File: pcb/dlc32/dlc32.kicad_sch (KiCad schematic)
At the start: 28 parts, among them IC1 74LV11, IC2 74HCT08, IC5 74HCT04, J1 DOOR1, J2 DOOR2, J3 CHILLER, J4 TO_J8, J6 Conn_02x04_Odd_Even, J7 LASER_AUX, J8 LASER

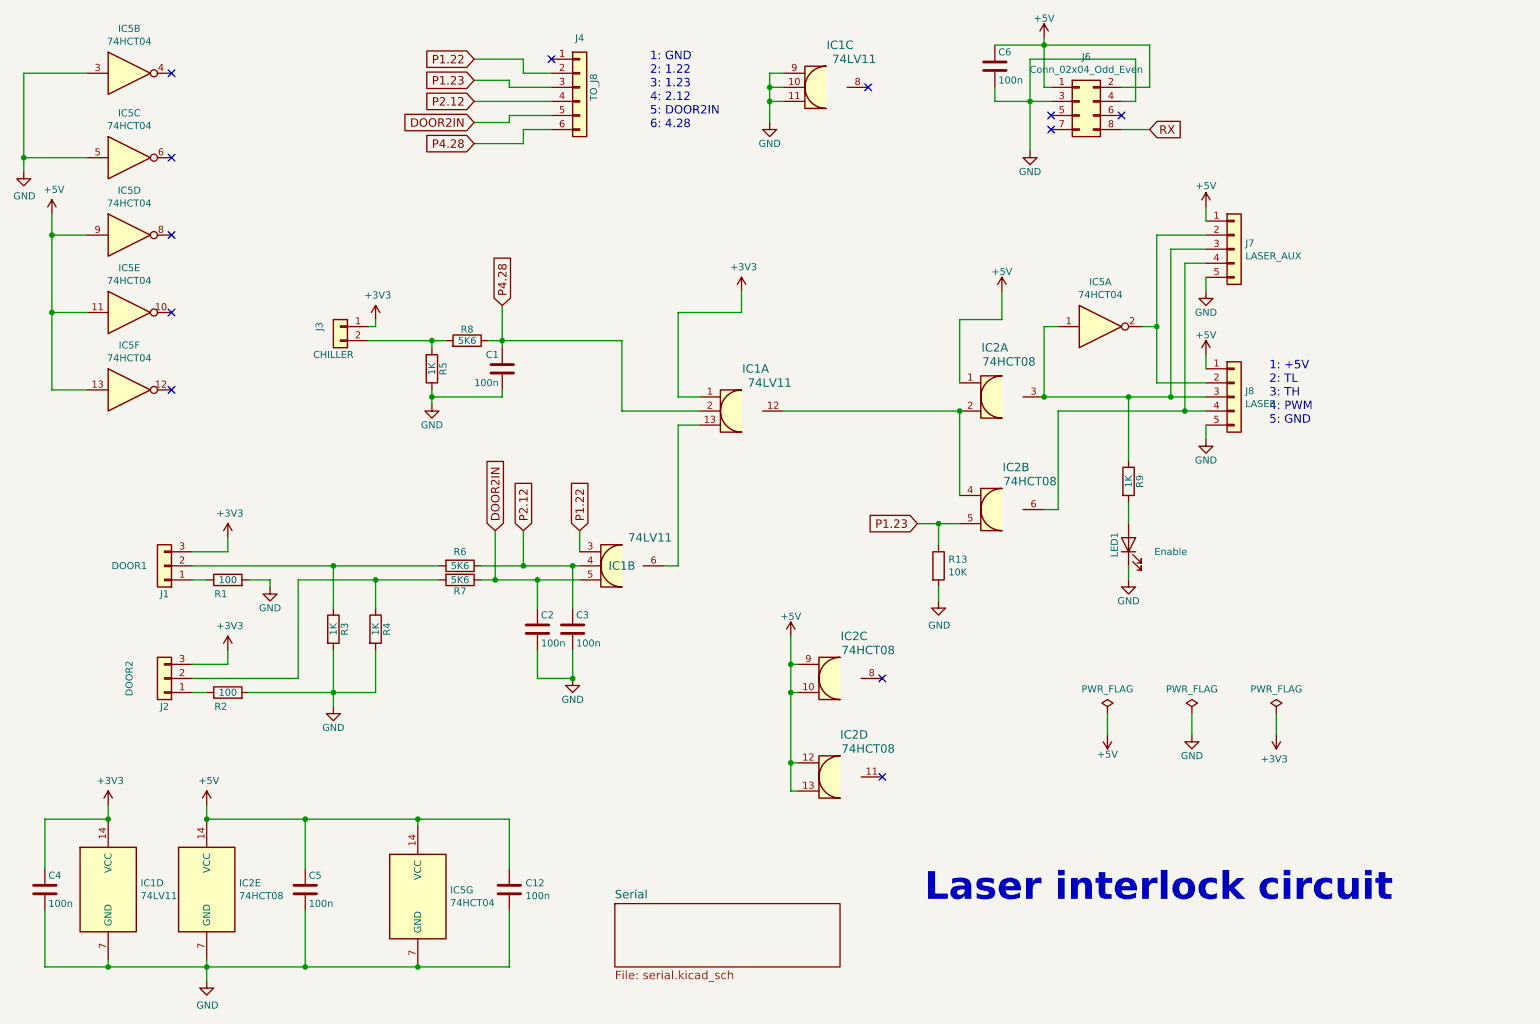
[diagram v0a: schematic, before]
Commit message: Update symbols etc, remove obsolete parts.
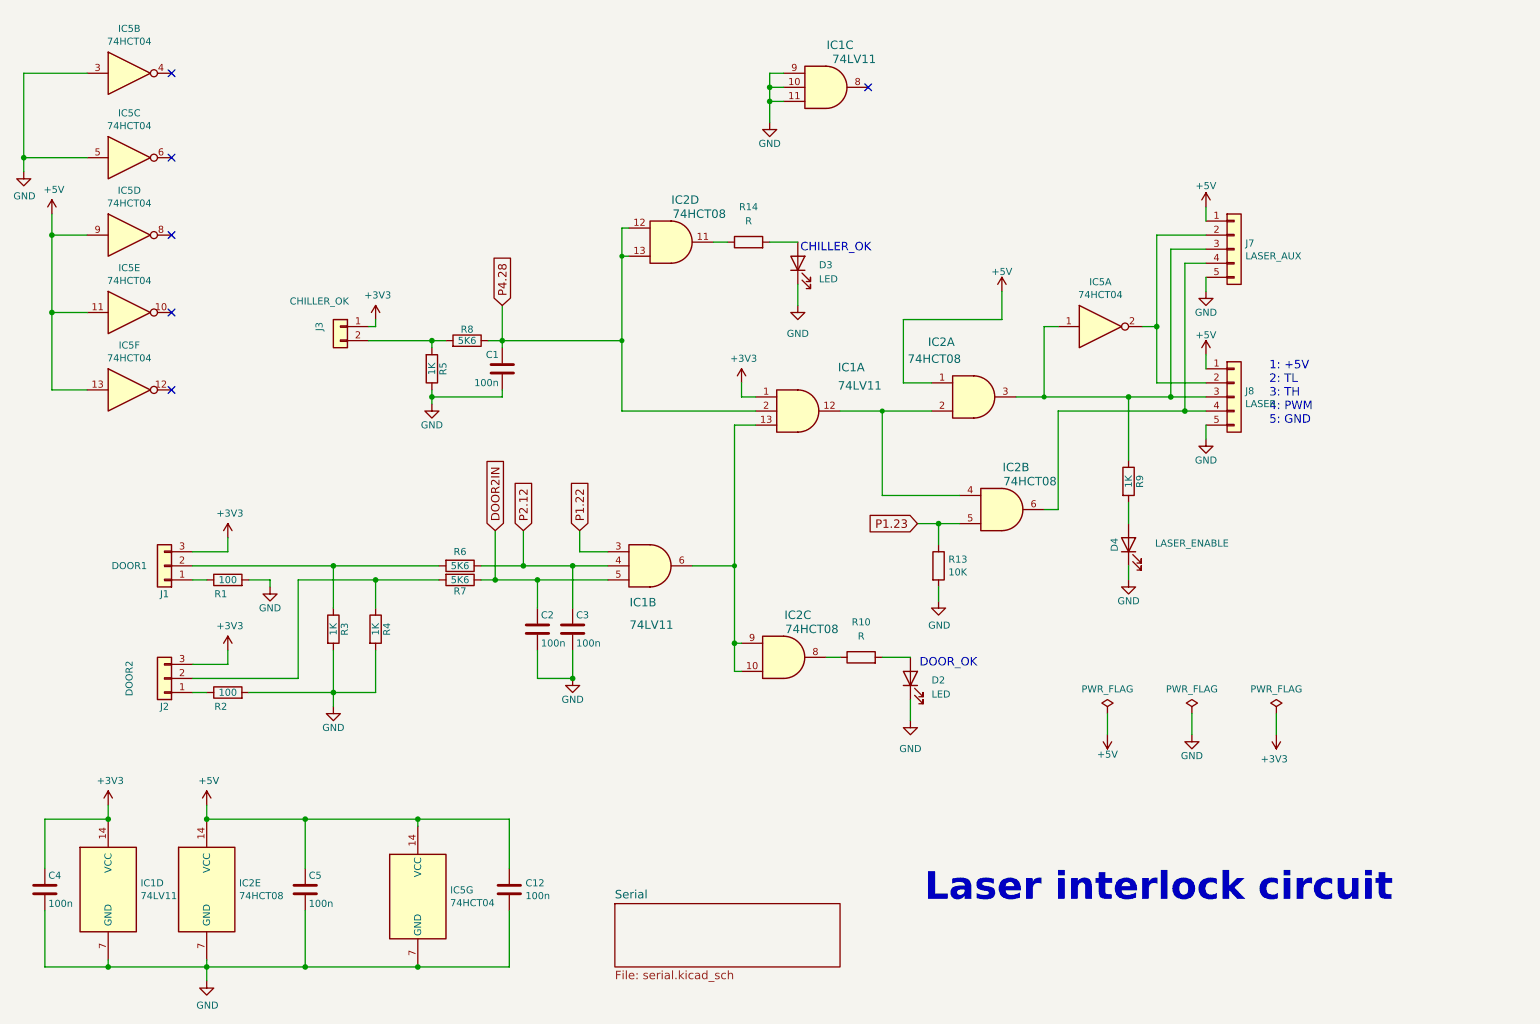
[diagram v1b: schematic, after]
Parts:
- removed C6: 100n, Capacitor_SMD:C_0603_1608Metric, symbol Device:C
- removed J4: TO_J8, Connector_JST:JST_XH_B06B-XH-A_1x06_P2.50mm_Vertical, symbol Connector_Generic:Conn_01x06
- removed J6: Conn_02x04_Odd_Even, Connector_PinSocket_2.54mm:PinSocket_2x04_P2.54mm_Vertical, symbol Connector_Generic:Conn_02x04_Odd_Even
- added D2, D3: LED, LED_THT:LED_D5.0mm_Horizontal_O1.27mm_Z3.0mm, symbol Device:LED
- added R10, R14: R, Resistor_SMD:R_0603_1608Metric, symbol Device:R
- D4: renamed from LED1; value Enable -> LASER_ENABLE; footprint LED_SMD:LED_0603_1608Metric -> LED_THT:LED_D5.0mm_Horizontal_O1.27mm_Z3.0mm
- J3: value CHILLER -> CHILLER_OK
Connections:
- net +5V: no longer IC2.10, IC2.12, IC2.13, IC2.9
- net GND: now also D2.1 (K), D3.1 (K)
- net P4.28: now also IC2.12, IC2.13
- net at IC1.13, IC1.6: now also IC2.10, IC2.9
- net at IC2.8: now also R10.1
- net at IC2.11: now also R14.1
- new net: D3.2 (A), R14.2
- new net: D2.2 (A), R10.2
- no-connect marks 12 -> 6
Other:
- note added: "CHILLER_OK"
- note added: "DOOR_OK"
- note removed: "1: GND 2: 1.22 3: 1.23 4: 2.12 5: DOOR2IN 6: 4.28"
- moved on the sheet: IC1A, IC1B, IC2A, IC2C

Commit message: Renumber, delete PCB.
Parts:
- renumbered C12 to C7, IC5 to IC3
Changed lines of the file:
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@@
 		(on_board yes)
 		(dnp no)
-		(property "Reference" "C12"
+		(property "Reference" "C7"
 			(at 108.331 172.8216 0)
 			(effects
@@
 			(project ""
 				(path "/fc0b2ef6-7d8e-4322-8468-8fac0c3c3d07"
-					(reference "C12")
+					(reference "C7")
 					(unit 1)
 				)
@@
 		(on_board yes)
 		(dnp no)
-		(property "Reference" "IC5"
+		(property "Reference" "IC3"
 			(at 36.83 18.6182 0)
 			(effects
@@
 			(project ""
 				(path "/fc0b2ef6-7d8e-4322-8468-8fac0c3c3d07"
-					(reference "IC5")
+					(reference "IC3")
 					(unit 2)
 				)
@@
 		(on_board yes)
 		(dnp no)
-		(property "Reference" "IC5"
+		(property "Reference" "IC3"
 			(at 36.83 33.8582 0)
 			(effects
@@
 			(project ""
 				(path "/fc0b2ef6-7d8e-4322-8468-8fac0c3c3d07"
-					(reference "IC5")
+					(reference "IC3")
 					(unit 3)
 				)
@@
 		(on_board yes)
 		(dnp no)
-		(property "Reference" "IC5"
+		(property "Reference" "IC3"
 			(at 36.83 47.8282 0)
 			(effects
@@
 			(project ""
 				(path "/fc0b2ef6-7d8e-4322-8468-8fac0c3c3d07"
-					(reference "IC5")
+					(reference "IC3")
 					(unit 4)
 				)
@@
 		(on_board yes)
 		(dnp no)
-		(property "Reference" "IC5"
+		(property "Reference" "IC3"
 			(at 36.83 61.7982 0)
 			(effects
@@
 			(project ""
 				(path "/fc0b2ef6-7d8e-4322-8468-8fac0c3c3d07"
-					(reference "IC5")
+					(reference "IC3")
 					(unit 5)
 				)
@@
 		(on_board yes)
 		(dnp no)
-		(property "Reference" "IC5"
+		(property "Reference" "IC3"
 			(at 36.83 75.7682 0)
 			(effects
@@
 			(project ""
 				(path "/fc0b2ef6-7d8e-4322-8468-8fac0c3c3d07"
-					(reference "IC5")
+					(reference "IC3")
 					(unit 6)
 				)

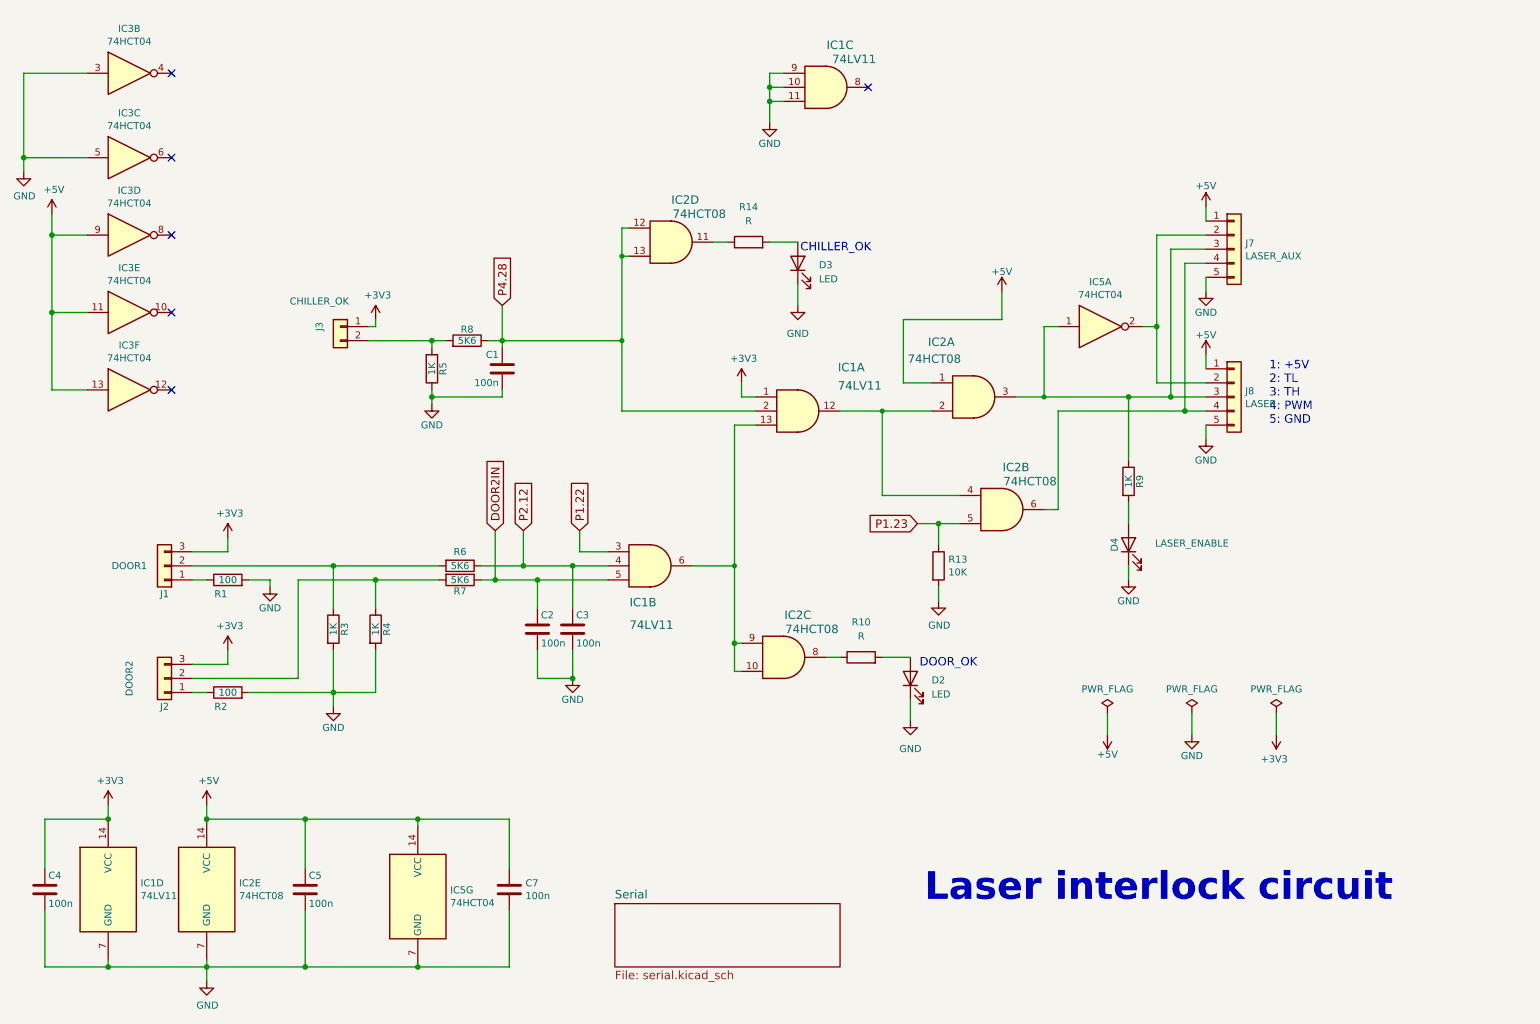
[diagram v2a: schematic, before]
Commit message: Include exhaust control in dlc32 pcb.
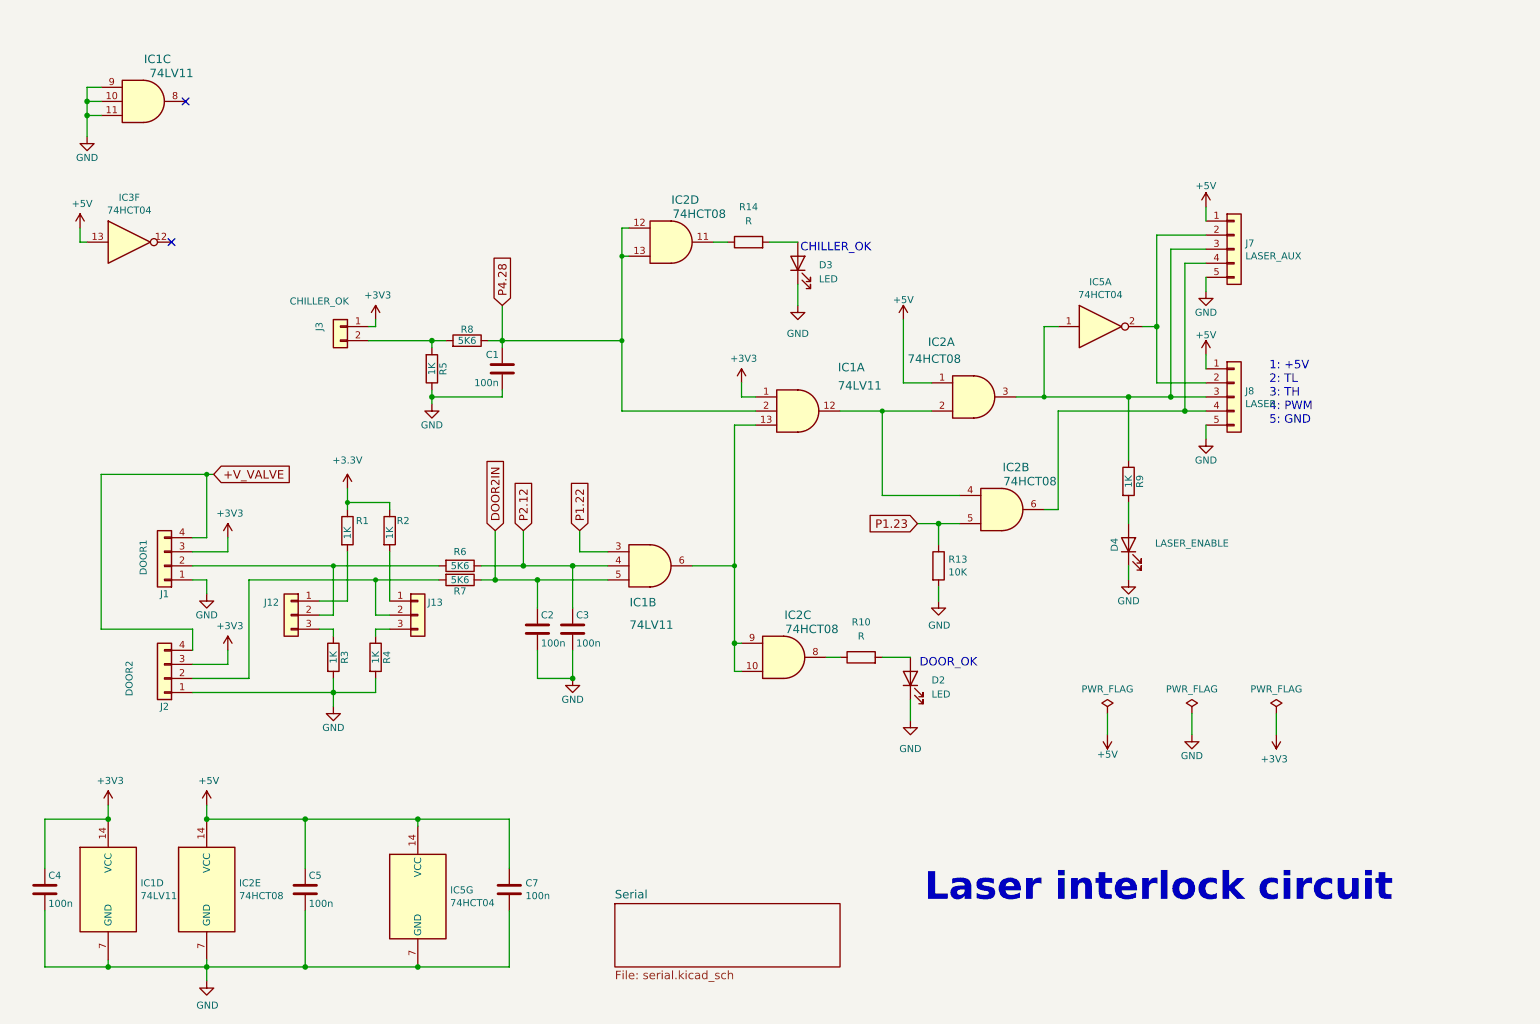
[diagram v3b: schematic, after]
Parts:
- removed unit 2 of IC3
- removed unit 3 of IC3
- removed unit 4 of IC3
- removed unit 5 of IC3
- added J12: Conn_01x03, Connector_PinHeader_2.54mm:PinHeader_1x03_P2.54mm_Vertical, symbol Connector_Generic:Conn_01x03
- added J13: Conn_01x03, Connector_JST:JST_XH_B3B-XH-A_1x03_P2.50mm_Vertical, symbol Connector_Generic:Conn_01x03
- J1, J2: footprint Connector_JST:JST_PH_B3B-PH-K_1x03_P2.00mm_Vertical -> Connector_JST:JST_XH_B4B-XH-A_1x04_P2.50mm_Vertical; symbol Connector_Generic:Conn_01x03 -> Connector_Generic:Conn_01x04
- J3: footprint Connector_JST:JST_PH_B2B-PH-K_1x02_P2.00mm_Vertical -> Connector_JST:JST_XH_B2B-XH-A_1x02_P2.50mm_Vertical
- J7, J8: footprint Connector_JST:JST_PH_B5B-PH-K_1x05_P2.00mm_Vertical -> Connector_JST:JST_XH_B5B-XH-A_1x05_P2.50mm_Vertical
- R1, R2: value 100 -> 1K
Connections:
- net GND: now also J1.1 (Pin_1), J2.1 (Pin_1); no longer R1.2, R2.2
- net at J1.2 (Pin_2), R6.2: now also J12.2 (Pin_2); no longer R3.1
- net at J2.2 (Pin_2), R7.2: now also J13.2 (Pin_2); no longer R4.1
- net +3.3V: now reaches R1.1
- net +3.3V: now also R2.1; no longer J1.1 (Pin_1)
- new net: J12.3 (Pin_3), R3.1
- new net: J13.3 (Pin_3), R4.1
- new net: J13.1 (Pin_1), R2.2
- new net: J12.1 (Pin_1), R1.2
- new net +V_VALVE: J1.4 (Pin_4), J2.4 (Pin_4)
- no-connect marks 6 -> 2
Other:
- moved on the sheet: IC1C, IC3F, R3, R4

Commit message: Simplify.
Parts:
- removed C4: 100n, Capacitor_SMD:C_0603_1608Metric, symbol Device:C
- removed IC1: 74LV11, Package_SO:SOIC-14_3.9x8.7mm_P1.27mm, symbol 74xx:74LS11
- renumbered C7 to C4, IC2 to IC1, IC5 to IC2, IC3 to IC2
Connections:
- net +3.3V is gone; now on net +5V: R1.1, R2.1
- net +3V3 is gone; now on net +5V: J1.3 (Pin_3), J2.3 (Pin_3), J3.1 (Pin_1)
- net P2.12 is gone; now on an unnamed net: C3.1, R6.1
- net +5V: now also D2.2 (A); no longer IC2.13
- net GND: no longer D2.1 (K)
- net at IC1.9: no longer IC1.10
- net at IC1.2, IC1.4: now also IC1.11
- net at IC1.8: now also IC1.13, IC2.13; no longer R10.1
- net at IC2.12: now also R10.1
- net at R14.1: now also D3.2 (A); no longer IC1.11
- net at R14.2: now also C1.1, IC1.12, R8.1; no longer D3.2 (A)
- net at R10.2: now also D2.1 (K); no longer D2.2 (A)
- net DOOR2IN: no longer names the net of C2.1, R7.1
- net DOOR2IN: now also IC1.10
- net P1.23 renamed LASER_PWM
- removed net P4.28: C1.1, IC1.12, IC1.13, R8.1
- no-connect marks 2 -> 0
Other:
- moved on the sheet: D2, D3, IC1C, IC1D, IC2F, R10, R14

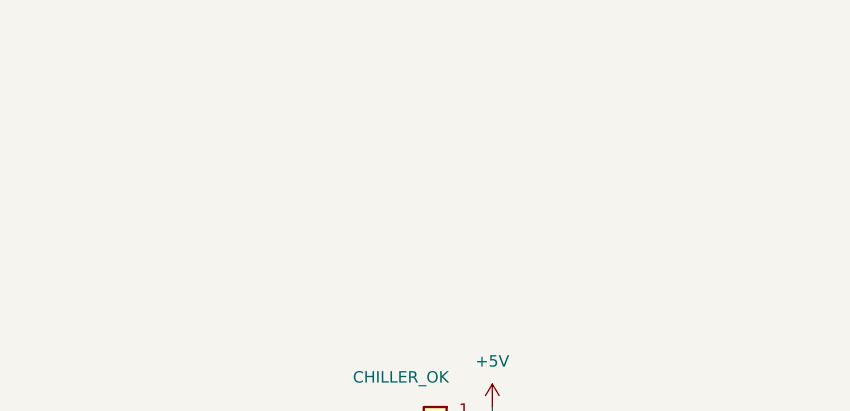
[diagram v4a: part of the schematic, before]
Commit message: Add mounting holes.
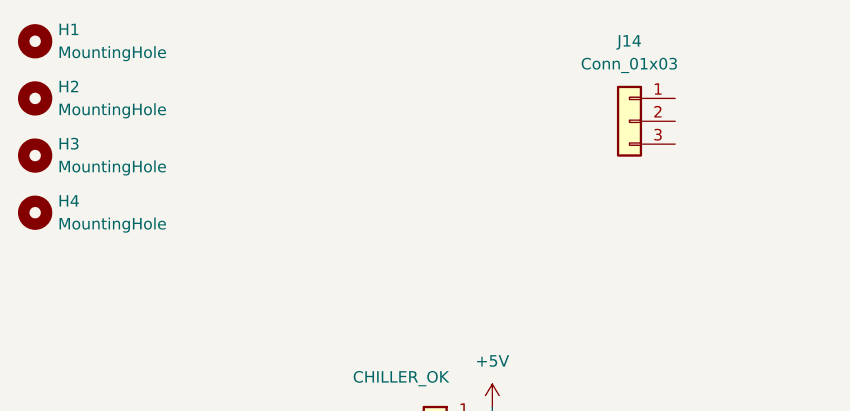
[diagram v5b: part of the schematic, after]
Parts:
- added H1, H2, H3, H4: MountingHole, MountingHole:MountingHole_3.2mm_M3, symbol Mechanical:MountingHole
- added J14: Conn_01x03, symbol Connector_Generic:Conn_01x03
